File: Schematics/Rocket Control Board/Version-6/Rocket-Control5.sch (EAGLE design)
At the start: 28 parts

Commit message: Another blog post + next order
Pics for the next blod post
Gerber files for the next PCB order. PLUS STENCIL
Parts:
- ANALOG-CAPACITOR-1, AREF-CAPACITOR-1, VDDCORE-CAPACITOR, VIN-CAPACITOR: DESC (none) -> CAP CER 0.1UF 10V X5R 0402; DIGIKEY# (none) -> 1276-1022-1-ND; MANF (none) -> Samsung Electro-Mechanics America, Inc.; MANF# (none) -> CL05A104KP5NNNC
- ANALOG-CAPACITOR-2, REGULATOR-IN-CAPACITOR: DESC (none) -> CAP CER 10UF 10V X5R 0402; DIGIKEY# (none) -> 1276-1450-1-ND; MANF (none) -> Samsung Electro-Mechanics America, Inc.; MANF# (none) -> CL05A106MP5NUNC
- AREF-CAPACITOR-2: DESC (none) -> CAP CER 0.47UF 10V X5R 0402; DIGIKEY# (none) -> 1276-1173-1-ND; MANF (none) -> Samsung Electro-Mechanics America, Inc.; MANF# (none) -> CL05A474KP5NNNC
- ARM-CORTEX-MO+: DESC (none) -> IC MCU 32BIT 256KB FLASH 48TQFP; DIGIKEY# (none) -> ATSAML21G18B-AUTCT-ND; MANF (none) -> Microchip Technology; MANF# (none) -> ATSAML21G18B-AUT
- CRYSTAL-CAP-1, CRYSTAL-CAP-2: DESC (none) -> CAP CER 6.8PF 50V NP0 0603; DIGIKEY# (none) -> 1276-2332-1-ND; MANF (none) -> Samsung Electro-Mechanics America, Inc.; MANF# (none) -> CL10C6R8BB8NNNC
- DIODE-USB, DIODE-VIN: DESC (none) -> DIODE SCHOTTKY 40V 500MA CST2; DIGIKEY# (none) -> CTS05S40L3FCT-ND; MANF (none) -> Toshiba Semiconductor and Storage; MANF# (none) -> CTS05S40,L3F
- FERRITE-BEAD: DESC (none) -> FERRITE BEAD 470 OHM 0603 1LN; DIGIKEY# (none) -> 490-5223-1-ND; MANF (none) -> Murata Electronics North America; MANF# (none) -> BLM18PG471SN1D
- HEADER-SIDE-A: DESC (none) -> CONN HEADER .100" SNGL STR 40POS; NOTE (none) -> One strip appears on the BOM.
- HEADER-SIDE-B: DESC (none) -> CONN HEADER .100" SNGL STR 40POS; DIGIKEY# (none) -> S1011EC-40-ND; MANF (none) -> Sullins Connector Solutions; MANF# (none) -> PRPC040SAAN-RC
- JTAG-CONNECTOR: DESC (none) -> CONN HEADER 10POS UNSHD VERT T/H; DIGIKEY# (none) -> 609-3712-ND; MANF (none) -> Amphenol FCI; MANF# (none) -> 20021111-00010T4LF
- LED-RESISTOR: DESC (none) -> RES SMD 330 OHM 5% 1/10W 0603; DIGIKEY# (none) -> 1276-5050-1-ND; MANF (none) -> Samsung Electro-Mechanics America, Inc.; MANF# (none) -> RC1608J331CS
- MICRO-USB-CONNECTOR: DESC (none) -> CONN USB MICRO B RECPT SMT R/A; DIGIKEY# (none) -> 609-4618-1-ND; MANF (none) -> Amphenol FCI; MANF# (none) -> 10118194-0001LF
- OSC-CRYSTAL: DESC (none) -> CRYSTAL 32.7680KHZ 6PF SMD; DIGIKEY# (none) -> 535-10240-1-ND; MANF (none) -> Abracon LLC; MANF# (none) -> ABS25-32.768KHZ-6-T
- POWER-LED: DESC (none) -> LED GREEN CLEAR 0603 SMD; DIGIKEY# (none) -> 754-1547-1-ND; MANF (none) -> Kingbright; MANF# (none) -> APTD1608ZGC
- REGULATOR-3.3V: DESC (none) -> IC REG BUCK 3.3V 0.5A SYNC 8WSON; DIGIKEY# (none) -> 296-39449-1-ND; MANF (none) -> Texas Instruments; MANF# (none) -> TPS62172DSGR
- REGULATOR-OUT-CAPACITOR: DESC (none) -> CAP CER 22UF 6.3V X5R 0402; DIGIKEY# (none) -> 1276-6834-1-ND; MANF (none) -> Samsung Electro-Mechanics America, Inc.; MANF# (none) -> CL05A226MQ5QUNC
- REGULATOR-OUT-INDUCTOR: DESC (none) -> FIXED IND 2.2UH 600MA 170 MOHM; DIGIKEY# (none) -> 445-3606-1-ND; MANF (none) -> TDK Corporation; MANF# (none) -> GLFR1608T2R2M-LR
- SCL-PULLUP, SDA-PULLUP: DESC (none) -> RES SMD 4.7K OHM 5% 1/10W 0603; DIGIKEY# (none) -> 1276-5078-1-ND; MANF (none) -> Samsung Electro-Mechanics America, Inc.; MANF# (none) -> RC1608J472CS
- SPI-PORT: NOTE (none) -> The 40 piece header fits the SPI port.
- VDDIO-1, VDDIO-2: device RocketControlBoard:RESISTORC0402 -> RocketControlBoard:CAPACITORC0402; DESC (none) -> CAP CER 0.1UF 10V X5R 0402; DIGIKEY# (none) -> 1276-1022-1-ND; MANF (none) -> Samsung Electro-Mechanics America, Inc.; MANF# (none) -> CL05A104KP5NNNC
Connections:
- net +3V3: now also VDDIO-1.B, VDDIO-2.B; no longer VDDIO-1.P$2, VDDIO-2.P$2
- net GND: now also VDDIO-1.A, VDDIO-2.A; no longer VDDIO-1.P$1, VDDIO-2.P$1

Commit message: Tons of Changes
Too many to describe. Most of the semester board design and rocket club
stuff.
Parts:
- removed OSC-CRYSTAL: ABS25-32.768KHZ-6-T, RocketControlBoard:ABS25-32.768KHZ-6-T
- added U$1: ABS07-32.768KHZ-T, RocketControlBoard:ABS07-32.768KHZ-T
- OSC-CAPACITOR-1, OSC-CAPACITOR-2: value 6.8pF -> 22pF; DESC CAP CER 6.8PF 50V NP0 0603 -> CAP CER 22PF 50V NP0 0603; DIGIKEY# 1276-2332-1-ND -> 1276-2229-1-ND; MANF# CL10C6R8BB8NNNC -> CL10C220JB8NNWC
- renumbered CRYSTAL-CAP-1 to OSC-CAPACITOR-2, CRYSTAL-CAP-2 to OSC-CAPACITOR-1
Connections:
- net CRYSTAL-A: now also U$1.P$2; no longer OSC-CRYSTAL.B
- net CRYSTAL-B: now also U$1.P$1; no longer OSC-CRYSTAL.A
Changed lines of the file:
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@@
 <attribute name="MANF#" value="ATSAML21G18B-AUT"/>
 </part>
-<part name="CRYSTAL-CAP-2" library="RocketControlBoard" deviceset="CAPACITOR" device="C0603" value="6.8pF">
-<attribute name="DESC" value="CAP CER 6.8PF 50V NP0 0603"/>
-<attribute name="DIGIKEY#" value="1276-2332-1-ND"/>
-<attribute name="MANF" value="Samsung Electro-Mechanics America, Inc."/>
-<attribute name="MANF#" value="CL10C6R8BB8NNNC"/>
-</part>
-<part name="CRYSTAL-CAP-1" library="RocketControlBoard" deviceset="CAPACITOR" device="C0603" value="6.8pF">
-<attribute name="DESC" value="CAP CER 6.8PF 50V NP0 0603"/>
-<attribute name="DIGIKEY#" value="1276-2332-1-ND"/>
-<attribute name="MANF" value="Samsung Electro-Mechanics America, Inc."/>
-<attribute name="MANF#" value="CL10C6R8BB8NNNC"/>
-</part>
 <part name="GND1" library="supply1" deviceset="GND" device=""/>
-<part name="OSC-CRYSTAL" library="RocketControlBoard" deviceset="ABS25-32.768KHZ-6-T" device="">
-<attribute name="DESC" value="CRYSTAL 32.7680KHZ 6PF SMD"/>
-<attribute name="DIGIKEY#" value="535-10240-1-ND"/>
-<attribute name="MANF" value="Abracon LLC"/>
-<attribute name="MANF#" value="ABS25-32.768KHZ-6-T"/>
-</part>
 <part name="GND2" library="supply1" deviceset="GND" device=""/>
 <part name="FERRITE-BEAD" library="RocketControlBoard" deviceset="BLM18PG471SN1D" device="">
@@
 <attribute name="MANF" value="Samsung Electro-Mechanics America, Inc."/>
 <attribute name="MANF#" value="CL05A106MP5NUNC"/>
+</part>
+<part name="U$1" library="RocketControlBoard" deviceset="ABS07-32.768KHZ-T" device=""/>
+<part name="OSC-CAPACITOR-1" library="RocketControlBoard" deviceset="CAPACITOR" device="C0603" value="22pF">
+<attribute name="DESC" value="CAP CER 22PF 50V NP0 0603"/>
+<attribute name="DIGIKEY#" value="1276-2229-1-ND"/>
+<attribute name="MANF" value="Samsung Electro-Mechanics America, Inc."/>
+<attribute name="MANF#" value="CL10C220JB8NNWC"/>
+</part>
+<part name="OSC-CAPACITOR-2" library="RocketControlBoard" deviceset="CAPACITOR" device="C0603" value="22pF">
+<attribute name="DESC" value="CAP CER 22PF 50V NP0 0603"/>
+<attribute name="DIGIKEY#" value="1276-2229-1-ND"/>
+<attribute name="MANF" value="Samsung Electro-Mechanics America, Inc."/>
+<attribute name="MANF#" value="CL10C220JB8NNWC"/>
 </part>
 </parts>
@@
 <attribute name="MANF#" x="38.1" y="68.58" size="1.778" layer="96" display="off"/>
 </instance>
-<instance part="CRYSTAL-CAP-2" gate="G$1" x="2.54" y="83.82">
-<attribute name="DESC" x="2.54" y="83.82" size="1.778" layer="96" display="off"/>
-<attribute name="DIGIKEY#" x="2.54" y="83.82" size="1.778" layer="96" display="off"/>
-<attribute name="MANF" x="2.54" y="83.82" size="1.778" layer="96" display="off"/>
-<attribute name="MANF#" x="2.54" y="83.82" size="1.778" layer="96" display="off"/>
-</instance>
-<instance part="CRYSTAL-CAP-1" gate="G$1" x="2.54" y="73.66">
-<attribute name="DESC" x="2.54" y="73.66" size="1.778" layer="96" display="off"/>
-<attribute name="DIGIKEY#" x="2.54" y="73.66" size="1.778" layer="96" display="off"/>
-<attribute name="MANF" x="2.54" y="73.66" size="1.778" layer="96" display="off"/>
-<attribute name="MANF#" x="2.54" y="73.66" size="1.778" layer="96" display="off"/>
-</instance>
 <instance part="GND1" gate="1" x="-12.7" y="71.12"/>
-<instance part="OSC-CRYSTAL" gate="G$1" x="15.24" y="78.74" rot="R90">
-<attribute name="DESC" x="15.24" y="78.74" size="1.778" layer="96" rot="R90" display="off"/>
-<attribute name="DIGIKEY#" x="15.24" y="78.74" size="1.778" layer="96" rot="R90" display="off"/>
-<attribute name="MANF" x="15.24" y="78.74" size="1.778" layer="96" rot="R90" display="off"/>
-<attribute name="MANF#" x="15.24" y="78.74" size="1.778" layer="96" rot="R90" display="off"/>
-</instance>
 <instance part="GND2" gate="1" x="-12.7" y="58.42"/>
 <instance part="FERRITE-BEAD" gate="G$1" x="2.54" y="35.56">
@@
 <attribute name="MANF#" x="2.54" y="43.18" size="1.778" layer="96" display="off"/>
 </instance>
+<instance part="U$1" gate="G$1" x="10.16" y="78.74" rot="R90"/>
+<instance part="OSC-CAPACITOR-1" gate="G$1" x="2.54" y="83.82">
+<attribute name="DESC" x="2.54" y="83.82" size="1.778" layer="96" display="off"/>
+<attribute name="DIGIKEY#" x="2.54" y="83.82" size="1.778" layer="96" display="off"/>
+<attribute name="MANF" x="2.54" y="83.82" size="1.778" layer="96" display="off"/>
+<attribute name="MANF#" x="2.54" y="83.82" size="1.778" layer="96" display="off"/>
+</instance>
+<instance part="OSC-CAPACITOR-2" gate="G$1" x="2.54" y="73.66">
+<attribute name="DESC" x="2.54" y="73.66" size="1.778" layer="96" display="off"/>
+<attribute name="DIGIKEY#" x="2.54" y="73.66" size="1.778" layer="96" display="off"/>
+<attribute name="MANF" x="2.54" y="73.66" size="1.778" layer="96" display="off"/>
+<attribute name="MANF#" x="2.54" y="73.66" size="1.778" layer="96" display="off"/>
+</instance>
 </instances>
 <busses>
@@
 <wire x1="38.1" y1="68.58" x2="20.32" y2="68.58" width="0.1524" layer="91"/>
 <wire x1="20.32" y1="68.58" x2="20.32" y2="86.36" width="0.1524" layer="91"/>
-<pinref part="OSC-CRYSTAL" gate="G$1" pin="B"/>
-<pinref part="CRYSTAL-CAP-2" gate="G$1" pin="B"/>
-<wire x1="15.24" y1="86.36" x2="10.16" y2="86.36" width="0.1524" layer="91"/>
 <wire x1="10.16" y1="86.36" x2="10.16" y2="83.82" width="0.1524" layer="91"/>
-<junction x="15.24" y="86.36"/>
-<wire x1="20.32" y1="86.36" x2="15.24" y2="86.36" width="0.1524" layer="91"/>
+<wire x1="20.32" y1="86.36" x2="10.16" y2="86.36" width="0.1524" layer="91"/>
+<pinref part="U$1" gate="G$1" pin="P$2"/>
+<pinref part="OSC-CAPACITOR-1" gate="G$1" pin="B"/>
+<junction x="10.16" y="83.82"/>
 </segment>
 </net>
@@
 <wire x1="38.1" y1="66.04" x2="15.24" y2="66.04" width="0.1524" layer="91"/>
 <wire x1="15.24" y1="66.04" x2="15.24" y2="71.12" width="0.1524" layer="91"/>
-<pinref part="OSC-CRYSTAL" gate="G$1" pin="A"/>
-<pinref part="CRYSTAL-CAP-1" gate="G$1" pin="B"/>
 <wire x1="15.24" y1="71.12" x2="10.16" y2="71.12" width="0.1524" layer="91"/>
 <wire x1="10.16" y1="71.12" x2="10.16" y2="73.66" width="0.1524" layer="91"/>
-<junction x="15.24" y="71.12"/>
+<pinref part="U$1" gate="G$1" pin="P$1"/>
+<pinref part="OSC-CAPACITOR-2" gate="G$1" pin="B"/>
+<junction x="10.16" y="73.66"/>
 </segment>
 </net>
@@
 <pinref part="GND1" gate="1" pin="GND"/>
 <wire x1="-12.7" y1="73.66" x2="-12.7" y2="76.2" width="0.1524" layer="91"/>
-<pinref part="CRYSTAL-CAP-2" gate="G$1" pin="A"/>
 <wire x1="-5.08" y1="83.82" x2="-7.62" y2="83.82" width="0.1524" layer="91"/>
 <wire x1="-7.62" y1="83.82" x2="-7.62" y2="76.2" width="0.1524" layer="91"/>
-<pinref part="CRYSTAL-CAP-1" gate="G$1" pin="A"/>
 <wire x1="-7.62" y1="76.2" x2="-7.62" y2="73.66" width="0.1524" layer="91"/>
 <wire x1="-7.62" y1="73.66" x2="-5.08" y2="73.66" width="0.1524" layer="91"/>
 <wire x1="-7.62" y1="76.2" x2="-12.7" y2="76.2" width="0.1524" layer="91"/>
 <junction x="-7.62" y="76.2"/>
+<pinref part="OSC-CAPACITOR-1" gate="G$1" pin="A"/>
+<pinref part="OSC-CAPACITOR-2" gate="G$1" pin="A"/>
 </segment>
 </net>

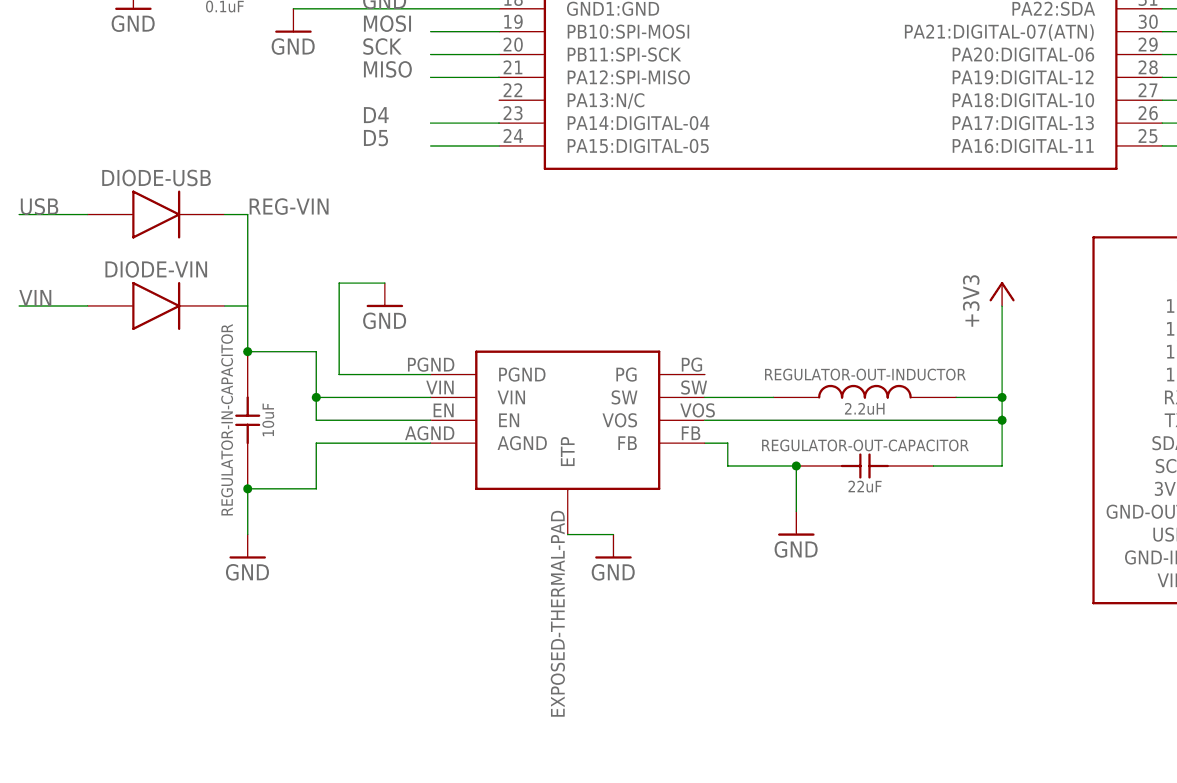
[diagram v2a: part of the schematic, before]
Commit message: New Crystal and Regualtor
Title
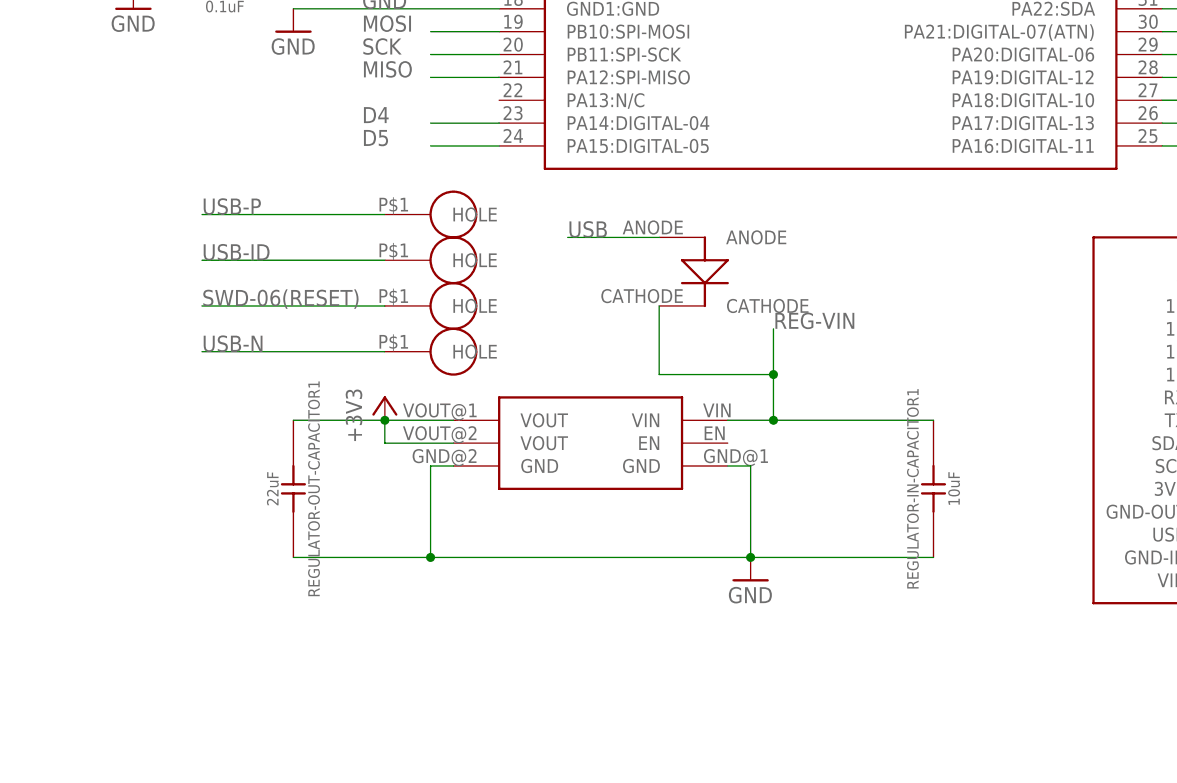
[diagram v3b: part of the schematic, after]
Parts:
- removed DIODE-USB, DIODE-VIN: CTS05S40,L3F, RocketControlBoard:CTS05S40,L3F
- removed REGULATOR-3.3V: TPS62172DSGR, RocketControlBoard:TPS62172DSGR
- removed REGULATOR-IN-CAPACITOR: 10uF, RocketControlBoard:CAPACITORC0402
- removed REGULATOR-OUT-CAPACITOR: 22uF, RocketControlBoard:CAPACITORC0402
- removed REGULATOR-OUT-INDUCTOR: 2.2uH, RocketControlBoard:INDUCTOR
- added REGULATOR-IN-CAPACITOR1: 10uF, RocketControlBoard:CAPACITORC0402
- added REGULATOR-OUT-CAPACITOR1: 22uF, RocketControlBoard:CAPACITORC0402
- added U$2: MIC5528, RocketControlBoard:MIC5528
- added U$3: DIODE-STANDARD, RocketControlBoard:DIODE-STANDARD
- added U$4, U$5, U$6, U$7: HEADER-HOLE, RocketControlBoard:HEADER-HOLE
- ARM-CORTEX-MO+: DIGIKEY# ATSAML21G18B-AUTCT-ND -> 1611-ATSAML21G18B-AUTCT-ND
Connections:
- removed net N$1: REGULATOR-3.3V.SW, REGULATOR-OUT-INDUCTOR.P$1
- net +3V3: now also REGULATOR-OUT-CAPACITOR1.A, U$2.VOUT@1, U$2.VOUT@2; no longer REGULATOR-3.3V.VOS, REGULATOR-OUT-CAPACITOR.B, REGULATOR-OUT-INDUCTOR.P$2
- net GND: now also REGULATOR-IN-CAPACITOR1.A, REGULATOR-OUT-CAPACITOR1.B, U$2.GND@1, U$2.GND@2; no longer REGULATOR-3.3V.AGND, REGULATOR-3.3V.ETP, REGULATOR-3.3V.FB, REGULATOR-3.3V.PGND, REGULATOR-IN-CAPACITOR.A, REGULATOR-OUT-CAPACITOR.A
- net REG-VIN: now also REGULATOR-IN-CAPACITOR1.B, U$2.VIN, U$3.CATHODE; no longer DIODE-USB.P$2, DIODE-VIN.P$2, REGULATOR-3.3V.EN, REGULATOR-3.3V.VIN, REGULATOR-IN-CAPACITOR.B
- net SWD-06(RESET): now also U$5.HOLE
- net USB: now also U$3.ANODE; no longer DIODE-USB.P$1
- net USB-ID: now also U$4.HOLE
- net USB-N: now also U$6.HOLE
- net USB-P: now also U$7.HOLE
- net VIN: no longer DIODE-VIN.P$1
